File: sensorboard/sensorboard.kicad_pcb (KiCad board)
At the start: 2 copper layers, 31.8 x 38.1 mm, 16 parts, among them P1 CONN_01X04, U1 LP38691, U2 MCP9808, U3 ABPMANN030PG2A3

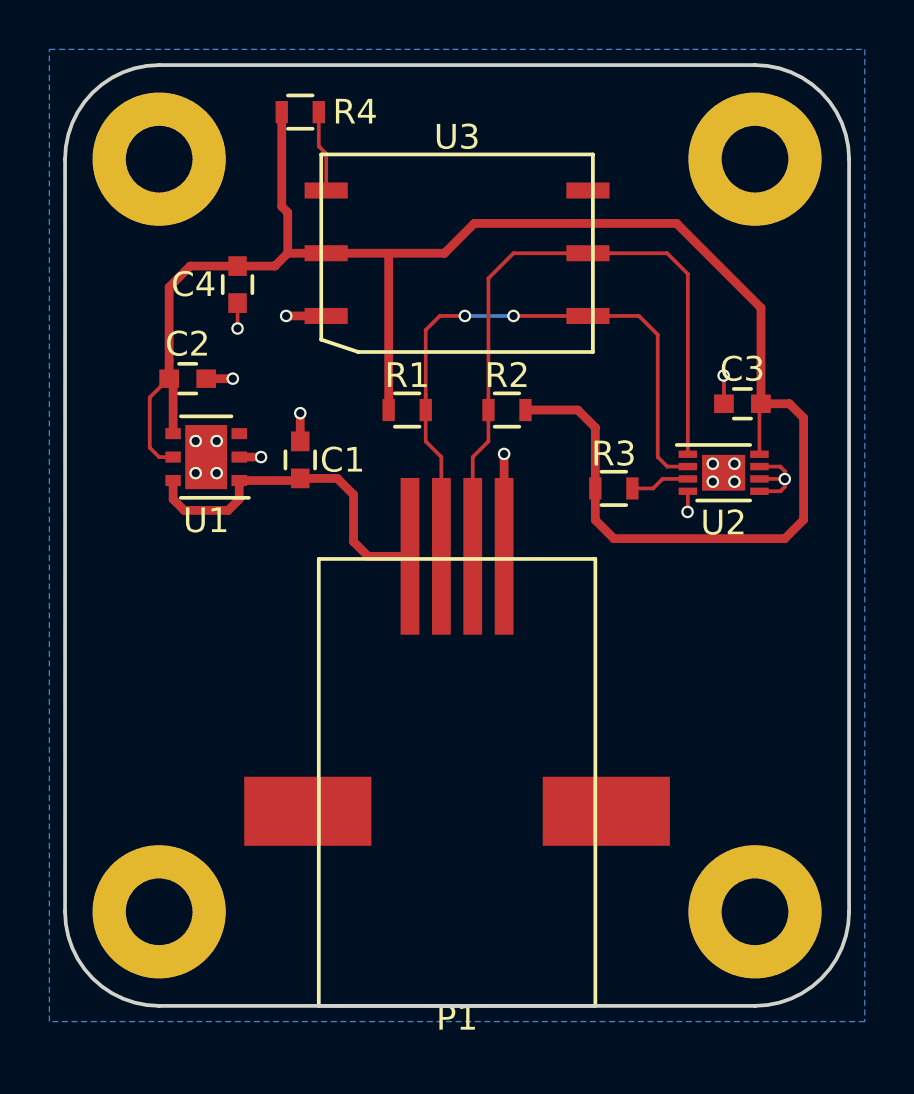
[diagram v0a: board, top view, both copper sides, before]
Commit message: Minor changes to sensor board layout
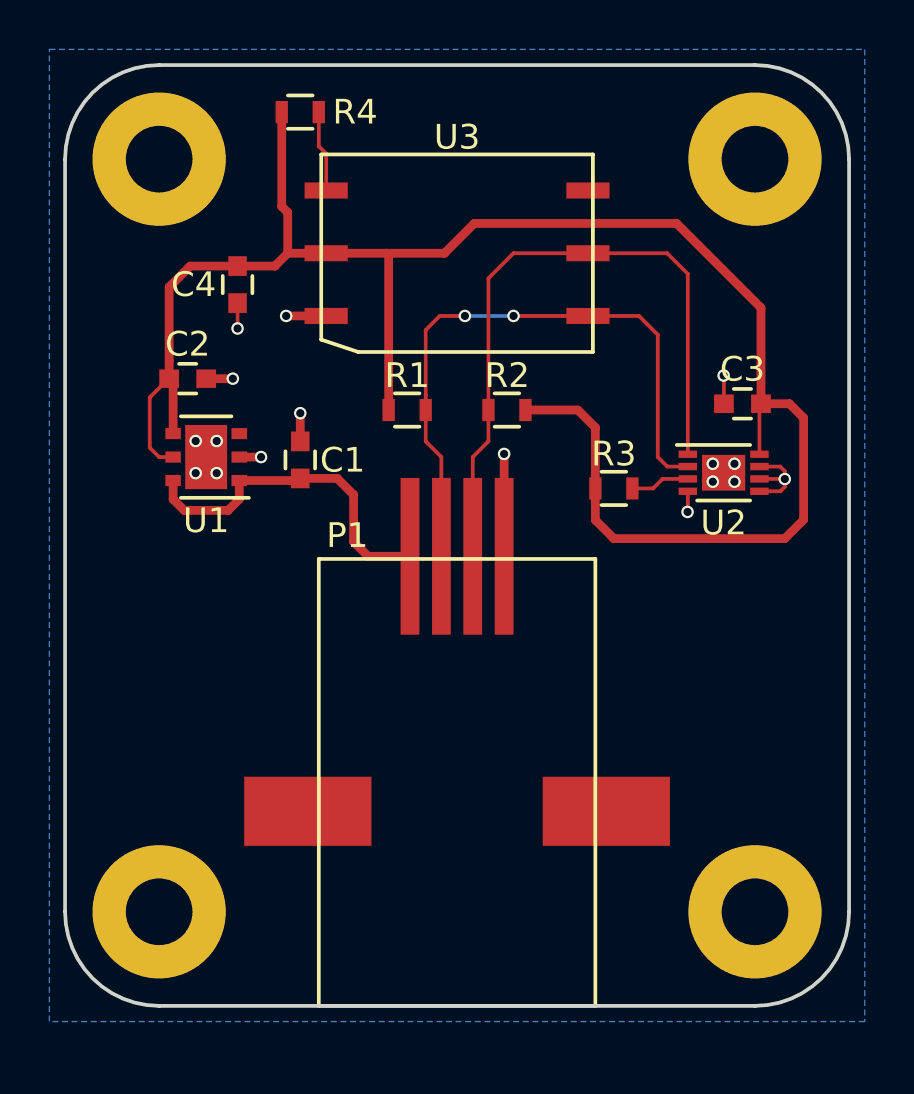
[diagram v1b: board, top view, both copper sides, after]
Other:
- rule pad_to_mask_clearance: 0.0762 -> 0.0254
- rule solder_mask_min_width: 0.1016 -> 0.0254
- board text added: "Kegerator Sensor Board"
- board text added: "https://github.com/jeffkub/beer-gauge"
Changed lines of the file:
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@@
     (links 39)
     (no_connects 0)
-    (area 136.449999 101.524999 168.350001 139.775001)
+    (area 128.250457 100.6326 176.549543 140.5174)
     (thickness 1.6)
-    (drawings 8)
+    (drawings 10)
     (tracks 116)
     (zones 0)
@@
     (pad_size 1.524 1.524)
     (pad_drill 0.762)
-    (pad_to_mask_clearance 0.0762)
-    (solder_mask_min_width 0.1016)
+    (pad_to_mask_clearance 0.0254)
+    (solder_mask_min_width 0.0254)
     (aux_axis_origin 0 0)
     (visible_elements 7FFFFF7F)
@@
   (module footprint:0855025005 (layer F.Cu)
     (at 152.4 139.7)
-    (fp_text reference P1 (at 0 0.5) (layer F.SilkS)
+    (fp_text reference P1 (at -4.445 -19.05) (layer F.SilkS)
       (effects (font (size 1 1) (thickness 0.15)))
     )
@@
     (pad 1 thru_hole circle (at 0 0) (size 5.4 5.4) (drill 2.7) (layers *.Cu *.Mask F.SilkS))
   )
+  (gr_text https://github.com/jeffkub/beer-gauge (at 152.4 123.19) (layer B.SilkS)
+    (effects (font (size 0.889 0.889) (thickness 0.2032)) (justify mirror))
+  )
+  (gr_text "Kegerator Sensor Board\n" (at 152.4 120.65) (layer B.SilkS)
+    (effects (font (size 1.5 1.5) (thickness 0.3)) (justify mirror))
+  )
   (gr_line (start 164.465 101.6) (end 140.335 101.6) (layer Edge.Cuts) (width 0.15))
